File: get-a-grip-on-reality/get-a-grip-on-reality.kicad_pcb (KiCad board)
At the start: 2 copper layers, 100 x 100 mm, 87 parts, among them J1 Conn_01x04_Pin, J10 MOTOR4, J11 MOTOR5, J12 Battery Connector MCU, J13 Conn_01x05_Pin, J14 Conn_01x05_Pin, J15 Battery Connector Bat, J2 HALL1, J3 HALL2, J4 HALL3, J5 HALL4, J6 HALL5, J7 MOTOR1, J8 MOTOR2, J9 MOTOR3, P1 USB_C_Plug_USB2.0, U1 TLV76733DRVx, U2 ESP32-S3-WROOM-1, U3 D3V3XA4B10LP, U4 IIM-42652, U5 TLV2462CDR, U6 BQ25887, U7 TPS54KB20RZRR

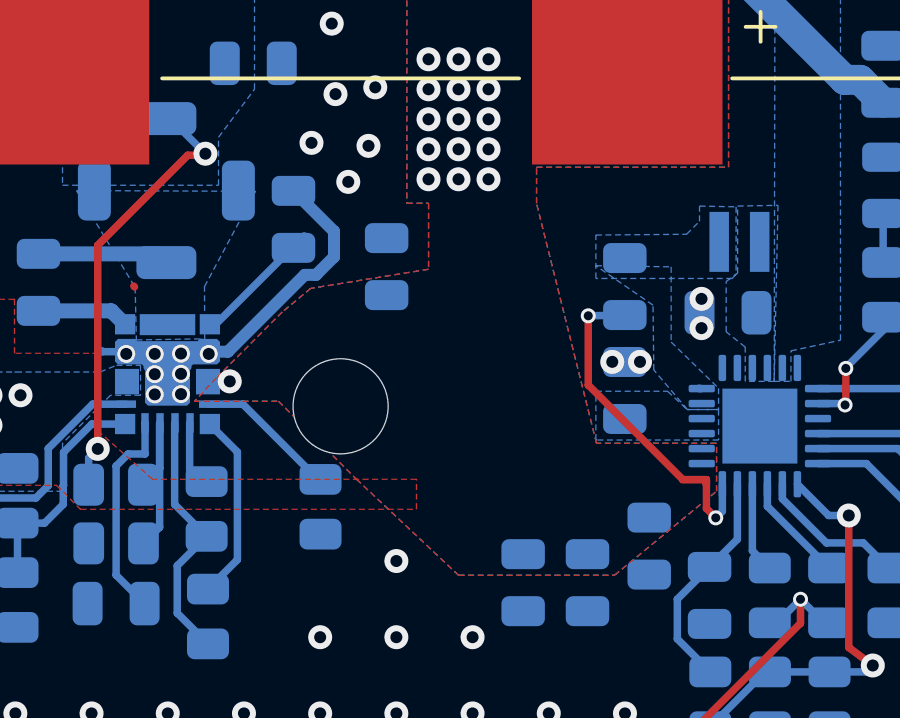
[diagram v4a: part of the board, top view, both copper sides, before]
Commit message: put designators in proper places
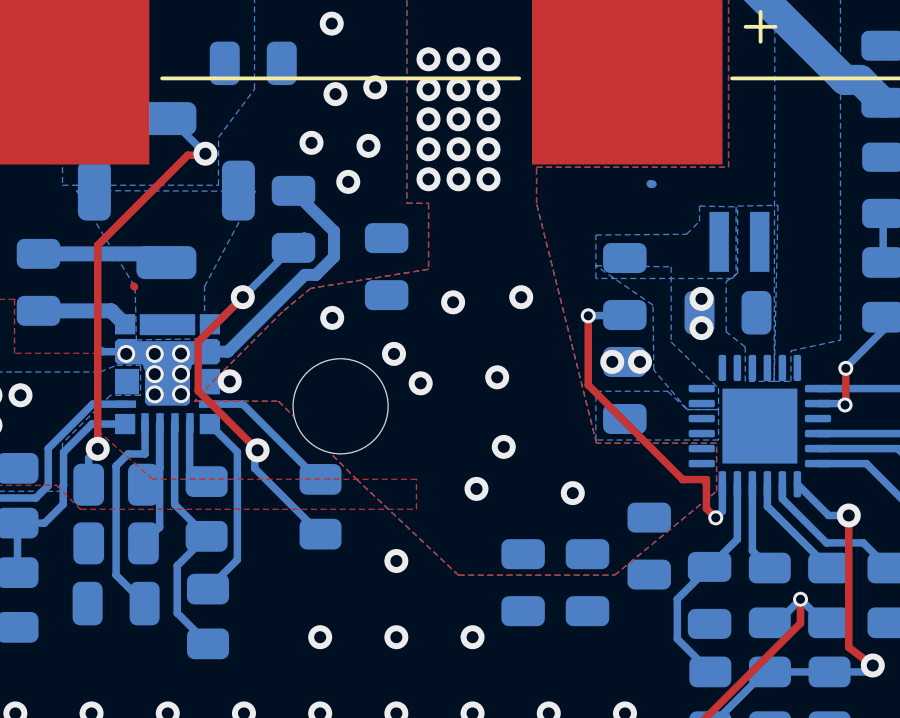
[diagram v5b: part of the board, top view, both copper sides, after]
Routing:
- net Net-(U7-VCC): track 4.55 -> 14.9 mm, vias 0 -> 2
- net GND: vias 705 -> 704
- net +BATT: vias 21 -> 30
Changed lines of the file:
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@@
 		(tags "resistor")
 		(property "Reference" "R15"
-			(at 0 1.65 90)
+			(at 6.941004 -0.1954 90)
 			(layer "B.SilkS")
 			(effects
@@
 			(layer "B.Fab")
 		)
-		(fp_text user "Designator506"
-			(at -2.286 3.5306 180)
-			(unlocked yes)
-			(layer "B.SilkS")
-			(effects
-				(font
-					(size 1 1)
-					(thickness 0.15)
-				)
-				(justify mirror)
-			)
-		)
 		(fp_text user "${REFERENCE}"
 			(at 0 0 180)
@@
 		(tags "capacitor")
 		(property "Reference" "C22"
-			(at 0 1.68 90)
+			(at -3.285 0.15 90)
 			(layer "B.SilkS")
 			(effects
@@
 		(tags "resistor")
 		(property "Reference" "R9"
-			(at 0 1.65 90)
+			(at 6.9772 -0.101026 90)
 			(layer "B.SilkS")
 			(effects
@@
 		(tags "capacitor")
 		(property "Reference" "C20"
-			(at 0 1.68 90)
+			(at -3.20985 0.025452 90)
 			(layer "B.SilkS")
 			(effects
@@
 		(tags "resistor")
 		(property "Reference" "TH1"
-			(at 0 1.65 90)
+			(at 6.9772 -0.101026 90)
 			(layer "B.SilkS")
 			(effects
@@
 		(tags "capacitor")
 		(property "Reference" "C28"
-			(at 0 1.68 0)
+			(at -2.7886 4.756204 0)
 			(layer "B.SilkS")
 			(effects
@@
 		(tags "resistor")
 		(property "Reference" "R18"
-			(at 0 1.65 90)
+			(at 6.9772 -0.101026 90)
 			(layer "B.SilkS")
 			(effects
@@
 		(tags "resistor")
 		(property "Reference" "R10"
-			(at 0 1.65 90)
+			(at 6.8975 -0.02 90)
 			(layer "B.SilkS")
 			(effects
@@
 		(tags "capacitor")
 		(property "Reference" "C26"
-			(at 0 1.68 90)
+			(at 6.8145 0.055626 90)
 			(layer "B.SilkS")
 			(effects
@@
 		(tags "LED")
 		(property "Reference" "D7"
-			(at 0 1.65 90)
+			(at -0.0296 1.865026 90)
 			(layer "B.SilkS")
 			(effects
@@
 		(tags "capacitor")
 		(property "Reference" "C24"
-			(at 0 1.68 90)
+			(at 6.9772 -0.071026 90)
 			(layer "B.SilkS")
 			(effects
@@
 		(tags "resistor")
 		(property "Reference" "R16"
-			(at 0 1.65 90)
+			(at 6.2975 -0.14 90)
 			(layer "B.SilkS")
 			(effects
@@
 		(tags "resistor")
 		(property "Reference" "R19"
-			(at 0 1.65 0)
+			(at -0.0247 5.910004 0)
 			(layer "B.SilkS")
 			(effects
@@
 		(tags "resistor")
 		(property "Reference" "R8"
-			(at 0 1.65 90)
+			(at -0.2244 -1.735026 90)
 			(layer "B.SilkS")
 			(effects
@@
 		(tags "capacitor")
 		(property "Reference" "C29"
-			(at 0 1.68 0)
+			(at 3.079548 -0.03485 0)
 			(layer "B.SilkS")
 			(effects
@@
 		(tags "inductor taiyo-yuden md smd")
 		(property "Reference" "L1"
-			(at 0 2 0)
+			(at -0.115426 3.9661 0)
 			(layer "B.SilkS")
 			(effects
@@
 		(tags "capacitor")
 		(property "Reference" "C16"
-			(at 0 1.68 90)
+			(at 3.2251 -0.100226 90)
 			(layer "B.SilkS")
 			(effects
@@
 		(tags "resistor")
 		(property "Reference" "R11"
-			(at 0 1.65 90)
+			(at 6.8975 -0.02 90)
 			(layer "B.SilkS")
 			(effects
@@
 		(tags "resistor")
 		(property "Reference" "R20"
-			(at 0 1.65 0)
+			(at 0 -5.444204 0)
 			(layer "B.SilkS")
 			(effects
@@
 		(tags "capacitor")
 		(property "Reference" "C21"
-			(at 0 1.68 0)
+			(at 0.017026 -4.8501 0)
 			(layer "B.SilkS")
 			(effects
@@
 		(tags "VQFN NoLead")
 		(property "Reference" "U6"
-			(at 0 3.33 0)
+			(at -1.864426 3.7258 0)
 			(layer "B.SilkS")
 			(effects
@@
 		(tags "capacitor")
 		(property "Reference" "C14"
-			(at 0 1.68 90)
+			(at -0.138 1.8094 90)
 			(layer "B.SilkS")
 			(effects
@@
 		(tags "resistor")
 		(property "Reference" "R12"
-			(at 0 1.65 90)
+			(at 6.9772 -0.101026 90)
 			(layer "B.SilkS")
 			(effects
@@
 		(tags "capacitor")
 		(property "Reference" "C19"
-			(at 0 1.68 90)
+			(at 3.2251 -0.100226 90)
 			(layer "B.SilkS")
 			(effects
@@
 		(tags "resistor")
 		(property "Reference" "R17"
-			(at 0 1.65 90)
+			(at 6.9772 -0.101026 90)
 			(layer "B.SilkS")
 			(effects
@@
 		(tags "capacitor")
 		(property "Reference" "C25"
-			(at 0 1.68 90)
+			(at 6.8145 0.055626 90)
 			(layer "B.SilkS")
 			(effects
@@
 		(tags "capacitor")
 		(property "Reference" "C30"
-			(at 0 1.68 0)
+			(at 3.344748 0.04775 0)
 			(layer "B.SilkS")
 			(effects
@@
 		(tags "resistor")
 		(property "Reference" "R13"
-			(at 0 1.65 90)
+			(at 6.9772 -0.101026 90)
 			(layer "B.SilkS")
 			(effects
@@
 		(tags "capacitor")
 		(property "Reference" "C15"
-			(at 0 1.68 90)
+			(at 3.2251 -0.100226 90)
 			(layer "B.SilkS")
 			(effects
@@
 		(tags "capacitor")
 		(property "Reference" "C17"
-			(at 0 1.68 90)
+			(at 6.8975 0.01 90)
 			(layer "B.SilkS")
 			(effects
@@
 		(tags "capacitor")
 		(property "Reference" "C23"
-			(at 0 1.68 0)
+			(at 0 -4.807604 0)
 			(layer "B.SilkS")
 			(effects
@@
 	)
 	(via
-		(at 104.975002 56.609999)
-		(size 0.6)
-		(drill 0.4)
-		(layers "F.Cu" "B.Cu")
-		(free yes)
-		(net 1)
-	)
-	(via
 		(at 83.789 33.725)
 		(size 0.5)
@@
 	)
 	(via
+		(at 114.81 59.71)
+		(size 0.8)
+		(drill 0.4)
+		(layers "F.Cu" "B.Cu")
+		(net 6)
+	)
+	(via
 		(at 97.7006 57.9882)
 		(size 0.8)
@@
 	)
 	(via
+		(at 113.9 61.11)
+		(size 0.8)
+		(drill 0.4)
+		(layers "F.Cu" "B.Cu")
+		(net 6)
+	)
+	(via
 		(at 112.3006 49.7882)
 		(size 0.8)
@@
 	)
 	(via
+		(at 109.09 55.41)
+		(size 0.8)
+		(drill 0.4)
+		(layers "F.Cu" "B.Cu")
+		(net 6)
+	)
+	(via
+		(at 115.39 54.72)
+		(size 0.8)
+		(drill 0.4)
+		(layers "F.Cu" "B.Cu")
+		(net 6)
+	)
+	(via
 		(at 114.3006 50.7882)
 		(size 0.8)
@@
 	)
 	(via
+		(at 117.11 61.25)
+		(size 0.8)
+		(drill 0.4)
+		(layers "F.Cu" "B.Cu")
+		(net 6)
+	)
+	(via
 		(at 113.3006 50.7882)
 		(size 0.8)
@@
 	)
 	(via
+		(at 113.12 54.89)
+		(size 0.8)
+		(drill 0.4)
+		(layers "F.Cu" "B.Cu")
+		(net 6)
+	)
+	(via
 		(at 105.675 57.525)
 		(size 0.8)
@@
 	)
 	(via
+		(at 114.59 57.39)
+		(size 0.8)
+		(drill 0.4)
+		(layers "F.Cu" "B.Cu")
+		(net 6)
+	)
+	(via
 		(at 97.7006 58.9882)
 		(size 0.8)
@@
 	)
 	(via
+		(at 111.15 56.61)
+		(size 0.8)
+		(drill 0.4)
+		(layers "F.Cu" "B.Cu")
+		(net 6)
+	)
+	(via
 		(at 96.7006 57.9882)
 		(size 0.8)
@@
 		(net 6)
 	)
+	(via
+		(at 112.04 57.59)
+		(size 0.8)
+		(drill 0.4)
+		(layers "F.Cu" "B.Cu")
+		(net 6)
+	)
 	(segment
 		(start 60.064 53.816)
@@
 	)
 	(segment
-		(start 121.408074 57.7658)
-		(end 121.331074 57.7658)
+		(start 119.7837 50.9513)
+		(end 119.7067 50.9513)
 		(width 0.25)
 		(layer "B.Cu")
@@
 	)
 	(segment
-		(start 121.331074 57.7658)
-		(end 121.317574 57.7523)
+		(start 119.7067 50.9513)
+		(end 119.6932 50.9378)
 		(width 0.25)
 		(layer "B.Cu")
@@
 	)
 	(segment
+		(start 104.625 57.845955)
+		(end 104.625 56.204698)
+		(width 0.25)
+		(layer "F.Cu")
+		(net 69)
+	)
+	(segment
+		(start 104.625 56.204698)
+		(end 106.109849 54.719849)
+		(width 0.25)
+		(layer "F.Cu")
+		(net 69)
+	)
+	(segment
+		(start 106.602454 59.823409)
+		(end 104.625 57.845955)
+		(width 0.25)
+		(layer "F.Cu")
+		(net 69)
+	)
+	(via
+		(at 106.109849 54.719849)
+		(size 0.8)
+		(drill 0.4)
+		(layers "F.Cu" "B.Cu")
+		(net 69)
+	)
+	(via
+		(at 106.602454 59.823409)
+		(size 0.8)
+		(drill 0.4)
+		(layers "F.Cu" "B.Cu")
+		(net 69)
+	)
+	(segment
+		(start 106.109849 54.719849)
+		(end 108.154548 52.67515)
+		(width 0.25)
+		(layer "B.Cu")
+		(net 69)
+	)
+	(segment
 		(start 108.7006 62.617196)
 		(end 108.529596 62.617196)
@@
 	)
 	(segment
+		(start 108.7006 62.617196)
+		(end 106.51 60.426596)
+		(width 0.25)
+		(layer "B.Cu")
+		(net 69)
+	)
+	(segment
 		(start 105.000899 55.623494)
 		(end 105.206204 55.623494)
@@
 	)
 	(segment
+		(start 106.51 60.426596)
+		(end 106.51 59.78)
+		(width 0.25)
+		(layer "B.Cu")
+		(net 69)
+	)
+	(segment
 		(start 105.206204 55.623494)
-		(end 108.154548 52.67515)
+		(end 106.109849 54.719849)
+		(width 0.25)
+		(layer "B.Cu")
+		(net 69)
+	)
+	(segment
+		(start 106.559045 59.78)
+		(end 106.602454 59.823409)
+		(width 0.25)
+		(layer "B.Cu")
+		(net 69)
+	)
+	(segment
+		(start 106.51 59.78)
+		(end 106.559045 59.78)
 		(width 0.25)
 		(layer "B.Cu")
